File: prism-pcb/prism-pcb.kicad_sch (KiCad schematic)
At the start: 0 parts

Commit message: tmc5130-uart -> prism-pcb
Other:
- title: tmc5130-uart -> prism-pcb
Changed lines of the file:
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@@
   (paper "A4")
   (title_block
-    (title "tmc5130-uart")
+    (title "prism-pcb")
     (date "2024-07-11")
     (rev "1.0")
@@
     )
     (instances
-      (project "tmc5130-uart"
+      (project "prism-pcb"
         (path "/df2b2e89-e055-4140-95de-f1df723db034" (page "4"))
       )
@@
     )
     (instances
-      (project "tmc5130-uart"
+      (project "prism-pcb"
         (path "/df2b2e89-e055-4140-95de-f1df723db034" (page "2"))
       )
@@
     )
     (instances
-      (project "tmc5130-uart"
+      (project "prism-pcb"
         (path "/df2b2e89-e055-4140-95de-f1df723db034" (page "3"))
       )

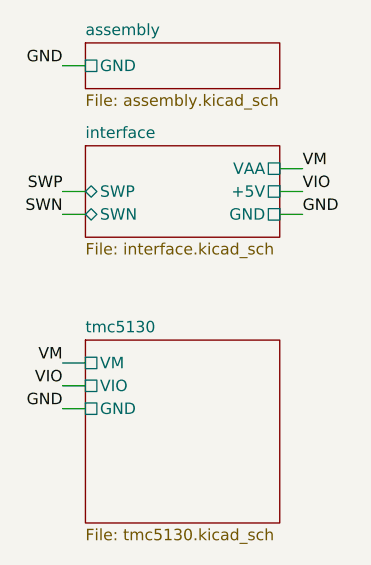
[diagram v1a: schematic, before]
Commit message: Update power supply connections
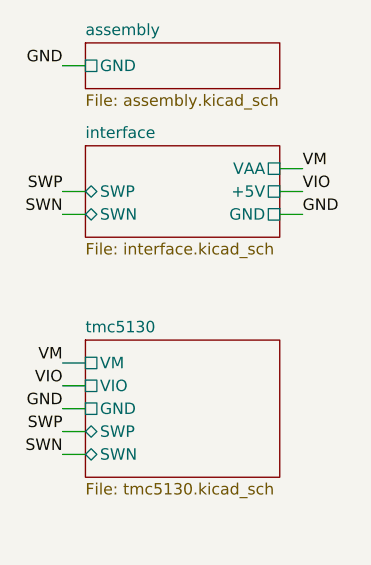
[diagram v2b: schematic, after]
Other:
- sheet tmc5130 ports: added SWN, SWP; removed none
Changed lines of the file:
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@@
+    (stroke (width 0) (type default))
+  )
+  (wire (pts (xy 130.81 96.52) (xy 128.27 96.52))
     (stroke (width 0) (type default))
   )
@@
     (stroke (width 0) (type default))
   )
+  (wire (pts (xy 130.81 99.06) (xy 128.27 99.06))
+    (stroke (width 0) (type default))
+  )
   (wire (pts (xy 154.94 69.85) (xy 152.4 69.85))
     (stroke (width 0) (type default))
@@
   (label "VIO" (at 154.94 69.85 0) (fields_autoplaced)
     (effects (font (size 1.27 1.27)) (justify left bottom))
+  )
+  (label "SWN" (at 128.27 99.06 180) (fields_autoplaced)
+    (effects (font (size 1.27 1.27)) (justify right bottom))
   )
   (label "VIO" (at 128.27 91.44 180) (fields_autoplaced)
@@
     (effects (font (size 1.27 1.27)) (justify right bottom))
   )
+  (label "SWP" (at 128.27 96.52 180) (fields_autoplaced)
+    (effects (font (size 1.27 1.27)) (justify right bottom))
+  )
   (label "VM" (at 154.94 67.31 0) (fields_autoplaced)
     (effects (font (size 1.27 1.27)) (justify left bottom))
   )
-  (sheet (at 130.81 86.36) (size 21.59 20.32) (fields_autoplaced)
+  (sheet (at 130.81 86.36) (size 21.59 15.24) (fields_autoplaced)
     (stroke (width 0.1524) (type solid))
     (fill (color 0 0 0 0.0000))
@@
       (effects (font (size 1.27 1.27)) (justify left bottom))
     )
-    (property "Sheetfile" "tmc5130.kicad_sch" (at 130.81 107.2646 0)
+    (property "Sheetfile" "tmc5130.kicad_sch" (at 130.81 102.1846 0)
       (effects (font (size 1.27 1.27)) (justify left top))
     )
@@
       (effects (font (size 1.27 1.27)) (justify left))
     )
+    (pin "SWN" bidirectional (at 130.81 99.06 180)
+      (effects (font (size 1.27 1.27)) (justify left))
+    )
+    (pin "SWP" bidirectional (at 130.81 96.52 180)
+      (effects (font (size 1.27 1.27)) (justify left))
+    )

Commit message: Place all footprints
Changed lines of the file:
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@@
     (effects (font (size 1.27 1.27)) (justify left bottom))
   )
-  (label "VIO" (at 154.94 69.85 0) (fields_autoplaced)
+  (label "+5V" (at 154.94 69.85 0) (fields_autoplaced)
     (effects (font (size 1.27 1.27)) (justify left bottom))
   )
@@
     (effects (font (size 1.27 1.27)) (justify right bottom))
   )
-  (label "VIO" (at 128.27 91.44 180) (fields_autoplaced)
+  (label "+5V" (at 128.27 91.44 180) (fields_autoplaced)
     (effects (font (size 1.27 1.27)) (justify right bottom))
   )
-  (label "VM" (at 128.27 88.9 180) (fields_autoplaced)
+  (label "VAA" (at 128.27 88.9 180) (fields_autoplaced)
     (effects (font (size 1.27 1.27)) (justify right bottom))
   )
@@
     (effects (font (size 1.27 1.27)) (justify right bottom))
   )
-  (label "VM" (at 154.94 67.31 0) (fields_autoplaced)
+  (label "VAA" (at 154.94 67.31 0) (fields_autoplaced)
     (effects (font (size 1.27 1.27)) (justify left bottom))
   )
